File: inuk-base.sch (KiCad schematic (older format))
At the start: 5 parts, among them U4 Logo_NM

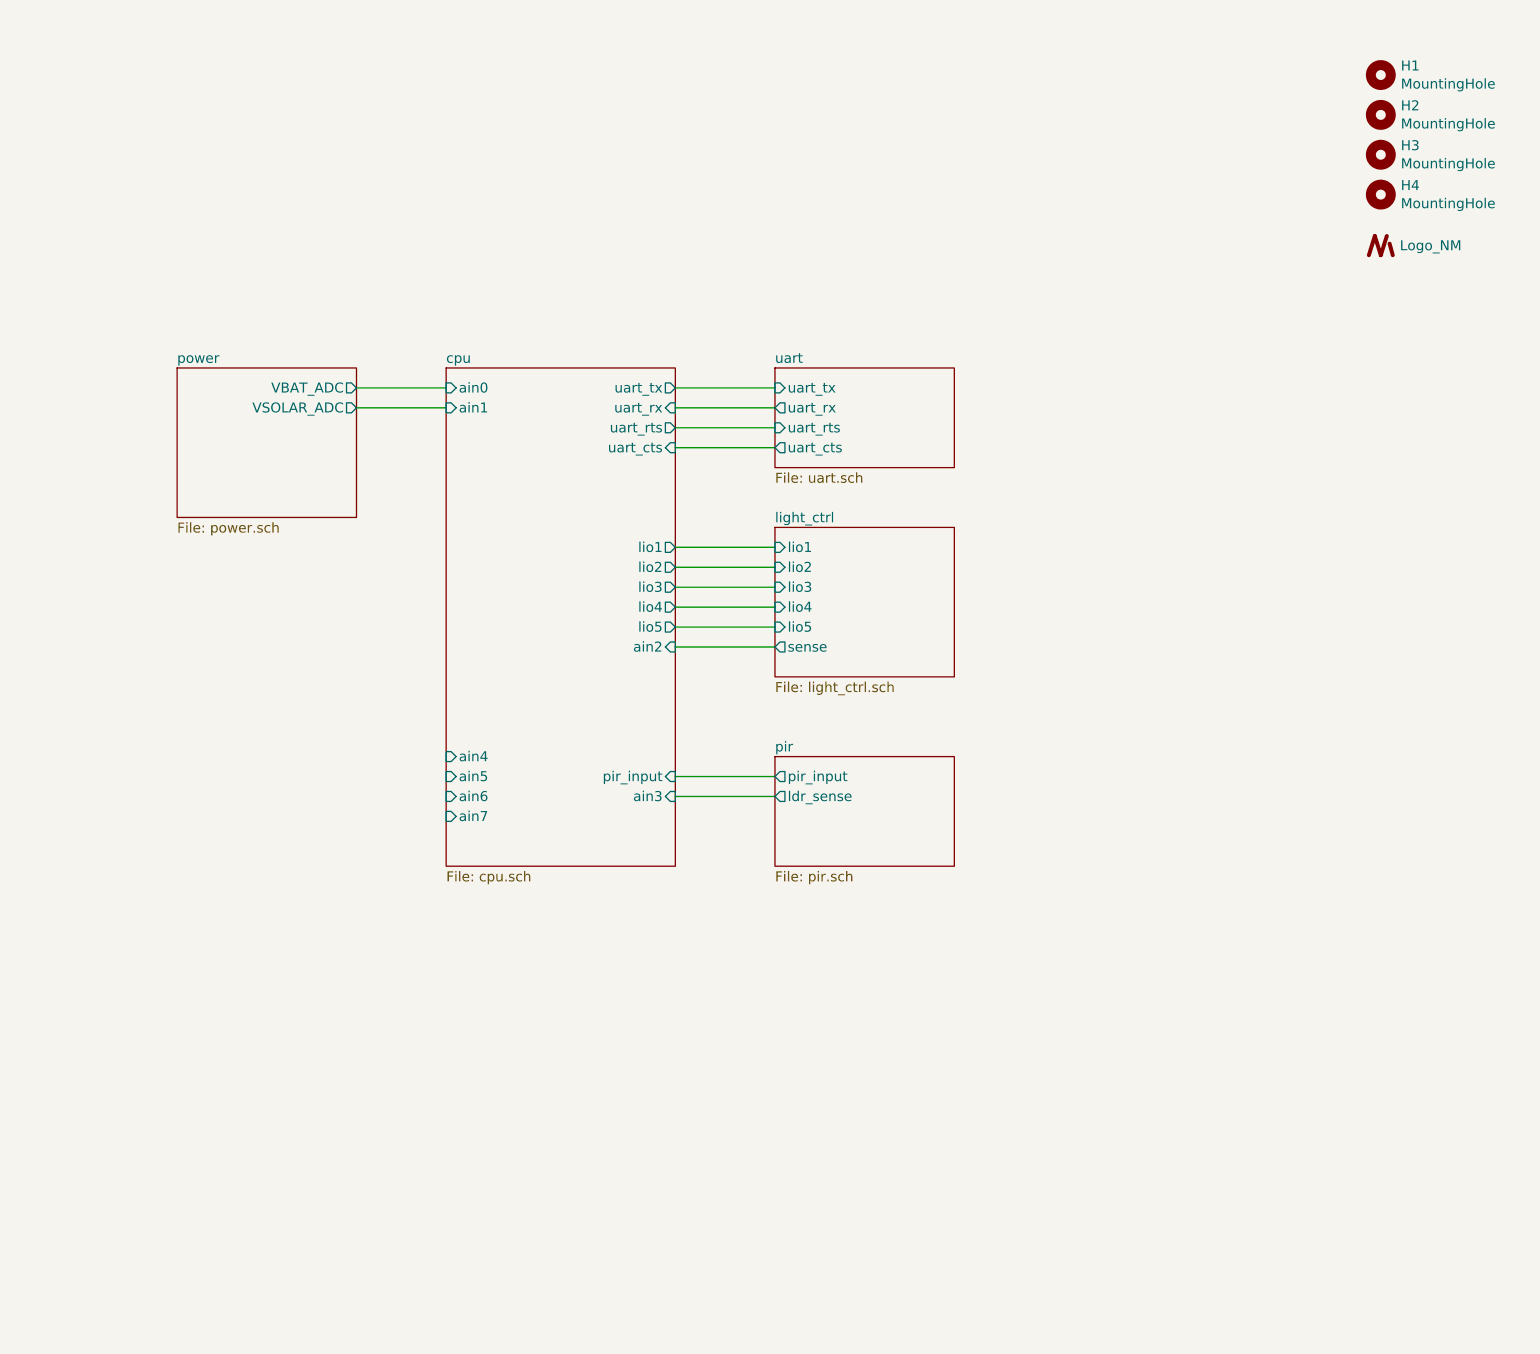
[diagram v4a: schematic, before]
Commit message: layout and more silk informations
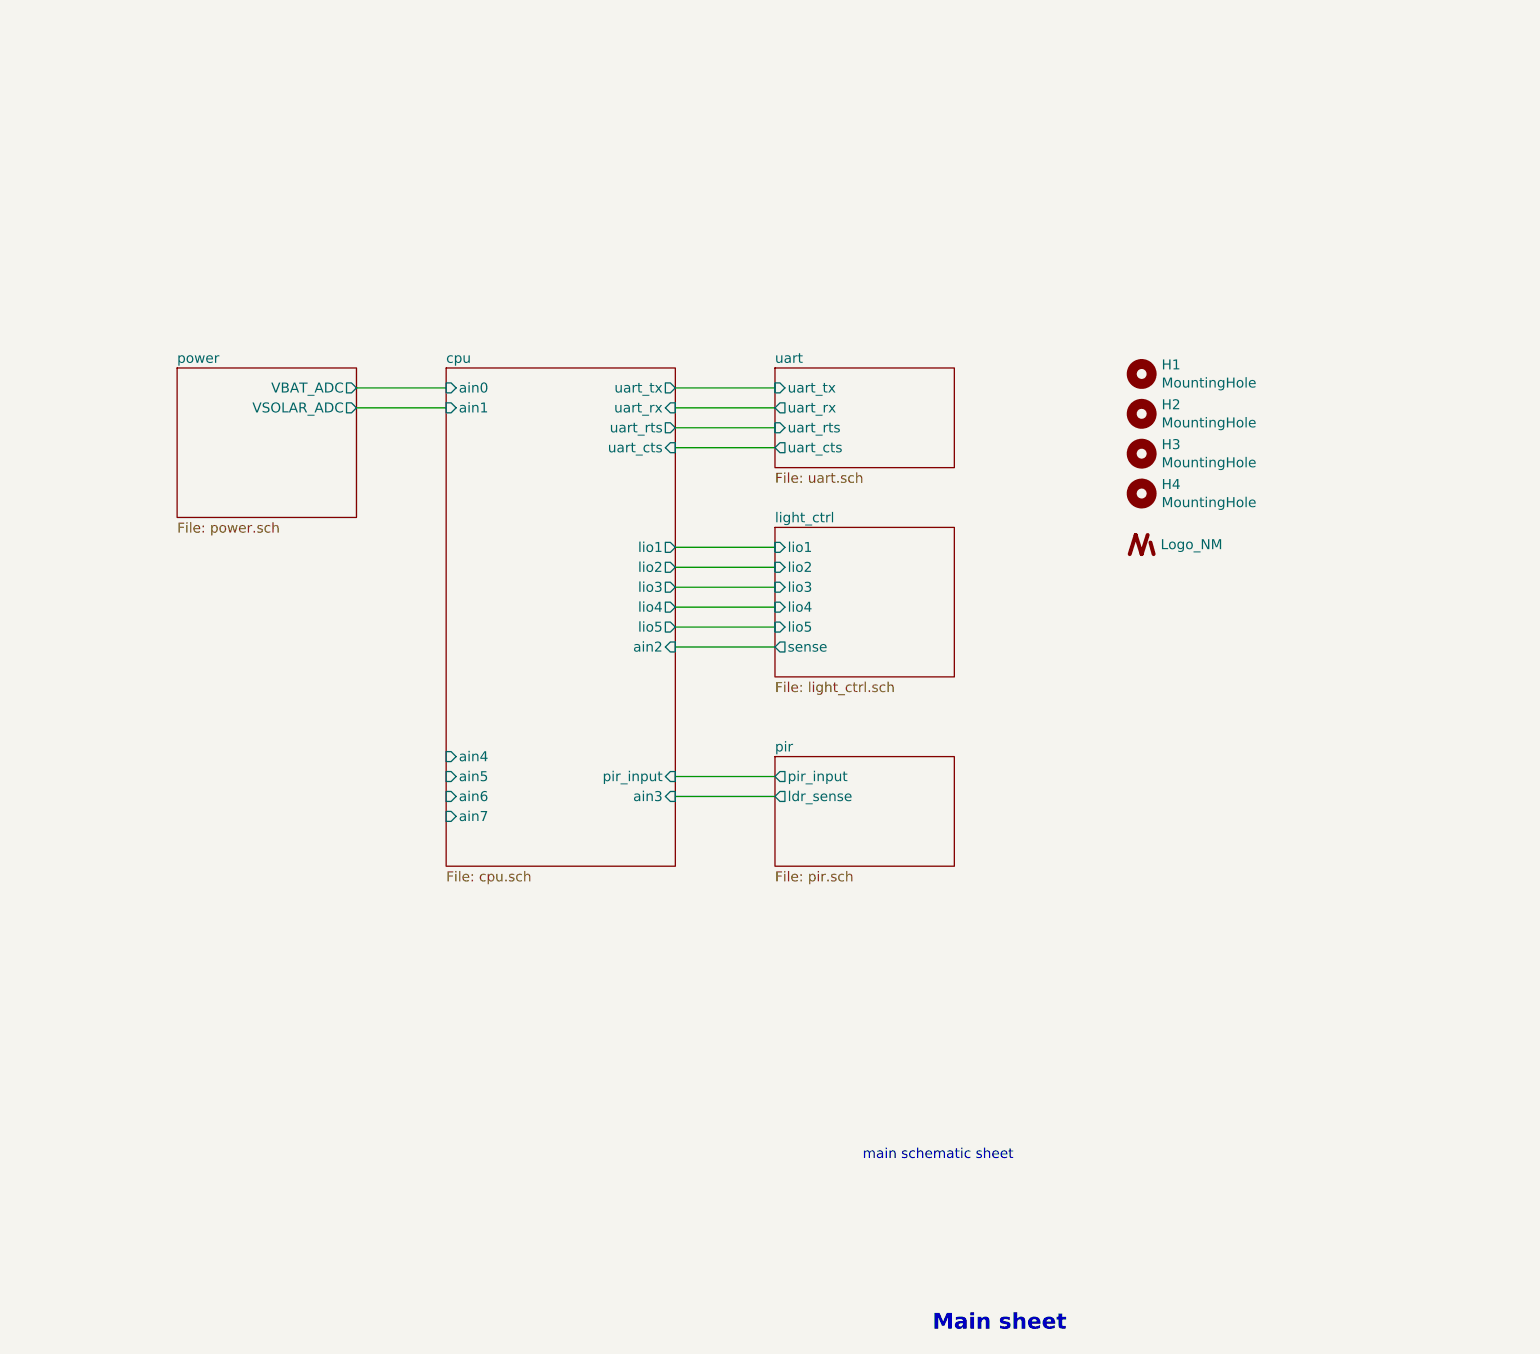
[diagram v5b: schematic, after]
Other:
- note added: "Main sheet"
- note added: "main schematic sheet"
- moved on the sheet: H1, H2, H3, H4
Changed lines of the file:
@@
 L Mechanical:MountingHole H4
 U 1 1 5E7D5F82
-P 9600 1800
-F 0 "H4" H 9700 1846 50  0000 L CNN
-F 1 "MountingHole" H 9700 1755 50  0000 L CNN
-F 2 "MountingHole:MountingHole_3.2mm_M3_Pad_Via" H 9700 1709 50  0001 L CNN
-F 3 "~" H 9600 1800 50  0001 C CNN
-	1    9600 1800
+P 8400 3300
+F 0 "H4" H 8500 3346 50  0000 L CNN
+F 1 "MountingHole" H 8500 3255 50  0000 L CNN
+F 2 "MountingHole:MountingHole_3.2mm_M3_Pad_Via" H 8500 3209 50  0001 L CNN
+F 3 "~" H 8400 3300 50  0001 C CNN
+	1    8400 3300
 	1    0    0    -1
 $EndComp
@@
 L Mechanical:MountingHole H3
 U 1 1 5E7D615B
-P 9600 1600
-F 0 "H3" H 9700 1646 50  0000 L CNN
-F 1 "MountingHole" H 9700 1555 50  0000 L CNN
-F 2 "MountingHole:MountingHole_3.2mm_M3_Pad_Via" H 9700 1509 50  0001 L CNN
-F 3 "~" H 9600 1600 50  0001 C CNN
-	1    9600 1600
+P 8400 3100
+F 0 "H3" H 8500 3146 50  0000 L CNN
+F 1 "MountingHole" H 8500 3055 50  0000 L CNN
+F 2 "MountingHole:MountingHole_3.2mm_M3_Pad_Via" H 8500 3009 50  0001 L CNN
+F 3 "~" H 8400 3100 50  0001 C CNN
+	1    8400 3100
 	1    0    0    -1
 $EndComp
@@
 L Mechanical:MountingHole H2
 U 1 1 5E7D677D
-P 9600 1400
-F 0 "H2" H 9700 1446 50  0000 L CNN
-F 1 "MountingHole" H 9700 1355 50  0000 L CNN
-F 2 "MountingHole:MountingHole_3.2mm_M3_Pad_Via" H 9700 1309 50  0001 L CNN
-F 3 "~" H 9600 1400 50  0001 C CNN
-	1    9600 1400
+P 8400 2900
+F 0 "H2" H 8500 2946 50  0000 L CNN
+F 1 "MountingHole" H 8500 2855 50  0000 L CNN
+F 2 "MountingHole:MountingHole_3.2mm_M3_Pad_Via" H 8500 2809 50  0001 L CNN
+F 3 "~" H 8400 2900 50  0001 C CNN
+	1    8400 2900
 	1    0    0    -1
 $EndComp
@@
 L Mechanical:MountingHole H1
 U 1 1 5E7D6AF7
-P 9600 1200
-F 0 "H1" H 9700 1246 50  0000 L CNN
-F 1 "MountingHole" H 9700 1155 50  0000 L CNN
-F 2 "MountingHole:MountingHole_3.2mm_M3_Pad_Via" H 9700 1109 50  0001 L CNN
-F 3 "~" H 9600 1200 50  0001 C CNN
-	1    9600 1200
+P 8400 2700
+F 0 "H1" H 8500 2746 50  0000 L CNN
+F 1 "MountingHole" H 8500 2655 50  0000 L CNN
+F 2 "MountingHole:MountingHole_3.2mm_M3_Pad_Via" H 8500 2609 50  0001 L CNN
+F 3 "~" H 8400 2700 50  0001 C CNN
+	1    8400 2700
 	1    0    0    -1
 $EndComp
@@
 L Custom:Logo_NM U4
 U 1 1 5EB7B6B6
-P 9600 2090
-F 0 "U4" H 9500 2140 50  0001 C CNN
-F 1 "Logo_NM" H 9695 2124 50  0000 L CNN
-F 2 "Custom:Logo_NM" H 9644 2020 50  0001 C CNN
-F 3 "" H 9540 2076 50  0001 C CNN
-	1    9600 2090
+P 8400 3590
+F 0 "U4" H 8300 3640 50  0001 C CNN
+F 1 "Logo_NM" H 8495 3624 50  0000 L CNN
+F 2 "Custom:Logo_NM" H 8444 3520 50  0001 C CNN
+F 3 "" H 8340 3576 50  0001 C CNN
+	1    8400 3590
 	1    0    0    -1
 $EndComp
+Text Notes 7350 7510 0    79   ~ 16
+Main sheet
+Text Notes 7000 6650 0    50   ~ 0
+main schematic sheet
 $EndSCHEMATC

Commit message: finished layout, created production files and added readme
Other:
- moved on the sheet: H4
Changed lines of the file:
@@
 L Mechanical:MountingHole H4
 U 1 1 5E7D5F82
-P 8400 3300
-F 0 "H4" H 8500 3346 50  0000 L CNN
-F 1 "MountingHole" H 8500 3255 50  0000 L CNN
-F 2 "MountingHole:MountingHole_3.2mm_M3_Pad_Via" H 8500 3209 50  0001 L CNN
-F 3 "~" H 8400 3300 50  0001 C CNN
-	1    8400 3300
+P 8400 3330
+F 0 "H4" H 8500 3376 50  0000 L CNN
+F 1 "MountingHole" H 8500 3285 50  0000 L CNN
+F 2 "MountingHole:MountingHole_3.2mm_M3_Pad_Via" H 8500 3239 50  0001 L CNN
+F 3 "~" H 8400 3330 50  0001 C CNN
+	1    8400 3330
 	1    0    0    -1
 $EndComp
@@
 L Mechanical:MountingHole H3
 U 1 1 5E7D615B
-P 8400 3100
-F 0 "H3" H 8500 3146 50  0000 L CNN
-F 1 "MountingHole" H 8500 3055 50  0000 L CNN
-F 2 "MountingHole:MountingHole_3.2mm_M3_Pad_Via" H 8500 3009 50  0001 L CNN
-F 3 "~" H 8400 3100 50  0001 C CNN
-	1    8400 3100
+P 8400 3110
+F 0 "H3" H 8500 3156 50  0000 L CNN
+F 1 "MountingHole" H 8500 3065 50  0000 L CNN
+F 2 "MountingHole:MountingHole_3.2mm_M3_Pad_Via" H 8500 3019 50  0001 L CNN
+F 3 "~" H 8400 3110 50  0001 C CNN
+	1    8400 3110
 	1    0    0    -1
 $EndComp
@@
 F7 "ain1" I L 4910 2870 50
 F8 "ain2" I R 6060 4070 50
-F9 "ain3" I R 6060 4820 50
-F10 "ain4" I L 4910 4620 50
-F11 "ain5" I L 4910 4720 50
-F12 "ain6" I L 4910 4820 50
-F13 "ain7" I L 4910 4920 50
-F14 "lio1" O R 6060 3570 50
-F15 "lio2" O R 6060 3670 50
-F16 "lio3" O R 6060 3770 50
-F17 "lio4" O R 6060 3870 50
-F18 "lio5" O R 6060 3970 50
-F19 "pir_input" I R 6060 4720 50
+F9 "ain4" I R 6060 4820 50
+F10 "lio1" O R 6060 3570 50
+F11 "lio2" O R 6060 3670 50
+F12 "lio3" O R 6060 3770 50
+F13 "lio4" O R 6060 3870 50
+F14 "lio5" O R 6060 3970 50
+F15 "pir_input" I R 6060 4720 50
 $EndSheet
 Wire Wire Line
